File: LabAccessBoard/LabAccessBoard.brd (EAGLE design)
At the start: 43.2 x 62.2 mm, 26 parts, among them CN1 6p-2.54, Q1 AO3400, X1 1751248

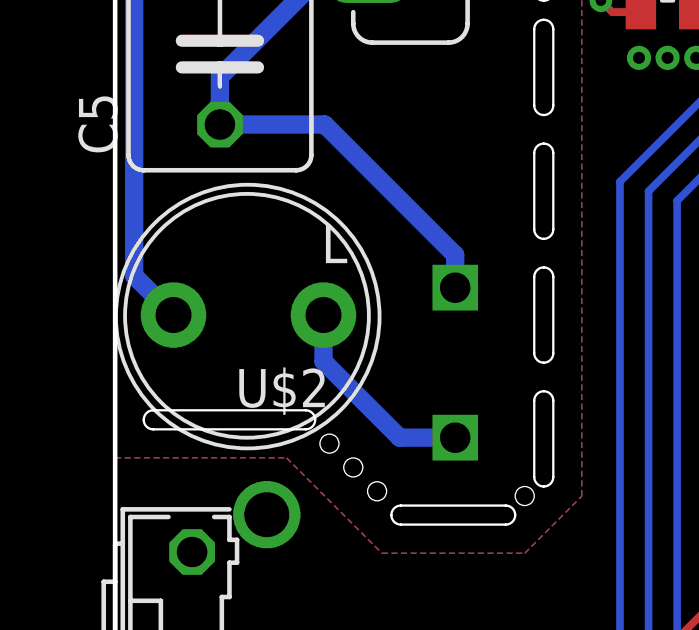
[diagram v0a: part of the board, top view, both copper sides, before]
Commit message: started firmware development
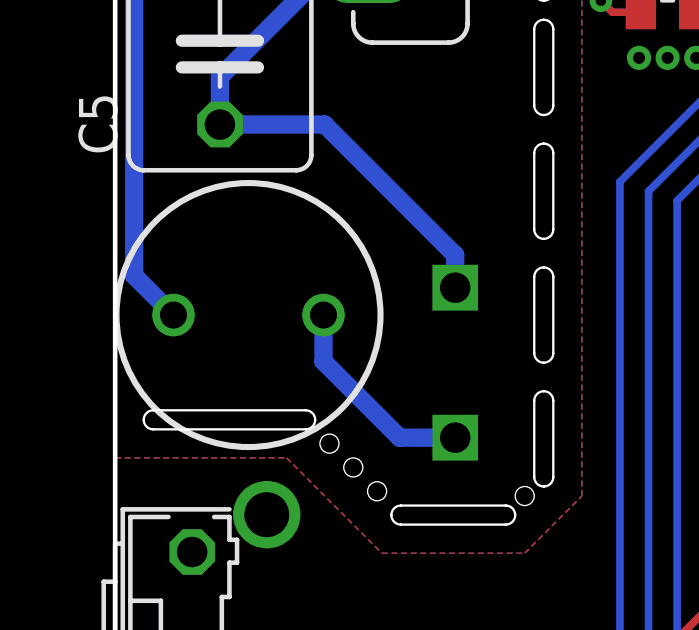
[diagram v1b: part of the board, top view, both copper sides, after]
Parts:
- U$2: value L -> (none); device adafruit:6000 -> rcl:6000-XXXX-RC
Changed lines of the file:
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@@
 <attribute name="SPICEPREFIX" value="C" x="3.4925" y="26.67" size="1.778" layer="27" rot="R90" display="off"/>
 </element>
-<element name="U$2" library="adafruit" library_urn="urn:adsk.eagle:library:420" package="6000" value="L" x="4.445" y="15.24" rot="R180"/>
+<element name="U$2" library="rcl" library_urn="urn:adsk.eagle:library:334" package="6000-XXXX-RC" package3d_urn="urn:adsk.eagle:package:23538/1" value="" x="4.445" y="15.24" smashed="yes" rot="R180">
+<attribute name="SPICEPREFIX" value="L" x="4.445" y="15.24" size="1.778" layer="27" rot="R180" display="off"/>
+<attribute name="VALUE" x="8.9506" y="21.6506" size="1.27" layer="27" rot="R180"/>
+</element>
 <element name="C6" library="rcl" library_urn="urn:adsk.eagle:library:334" package="C0805K" package3d_urn="urn:adsk.eagle:package:23681/2" value="22uF" x="26.3525" y="29.845" rot="R180">
 <attribute name="SPICEPREFIX" value="C" x="26.3525" y="29.845" size="1.778" layer="27" rot="R180" display="off"/>
